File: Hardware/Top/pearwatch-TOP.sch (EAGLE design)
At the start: 49 parts, among them U2 NRF52832_MODULE_MDBT42, U4 PCF8523

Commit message: adding updated top board
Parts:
- added SW1, SW2: SWITCH.MOM, LinnesLab-Switches:SWITCH.MOM
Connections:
- net GND: now also USB2.SHIELD
- net N$5: now also C14.2, D1.A, R5.1
- net RESET: no longer C14.2, D1.A, R5.1
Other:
- note added: "Cortext Debugger"
- note added: "Digital Outputs CS.OLED RESET.OLED DC.OLED Digital Inputs 3x buttons Charge Status Analog Inputs Battery monitor Analog Outputs"
- note added: "Power Management"
- note added: "SD Card"
- note added: "buttons"
- note added: "nRF52832 Module"
- note added: "real time clock"
- note removed: "Additional notes for advanced users only"
- note removed: "PIN_DFU / P0.20: If this pin is detected to be at GND level at startup, the board will enter a special serial bootloader mode and will not execute any user code, going straight into bootloader mode. If you wish to use this pin as a standard GPIO, make sure that it is pulled high with a pullup resistor so that your code will execute normally when the MCU starts up. FRST/P0.22: Setting this pin to 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"
- note removed: "SPECIAL / PORT / PIN ON PACKAGE / GPIO(D_or_A) / Comments Factory Reset / P0.22 / pin38 / DO NOT USE FOR ANY GPIO SWDIO / none / pin37 / reserved-not available for general GPIO SWCLK / none / pin36 / reserved-not available for general GPIO RESET / P0.21 / pin35 / reserved-not available for general GPIO DFU / P0.20 / pin34 / reserved-not available for general GPIO LED2 / P0.19 / pin33 / reserved f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"
- note removed: "SPECIAL / PORT / PIN ON PACKAGE / GPIO(D_or_A) / Comments none / P0.02 / pin15 / D2_or_A0 none / P0.03 / pin16 / D3_or_A1 none / P0.04 / pin17 / D4_or_A2 none / P0.05 / pin18 / D5_or_A3 TXD / P0.06 / pin19 / D6 / but reserved for Serial communication and programming none / P0.07 / pin20 / D7 RXD / P0.08 / pin21 / D8 / but reserved for Serial communication and programming NFC1 / P0.09 / pin22 / D9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"
- note removed: "Some pins are noted as reserved and not available for general GPIO (unless you are an adavanced user) I2C, SPI, and SWD pins can be repurposed if you know what you are doing For Milestones, avoid repurposing NFC pins. For P0.19 (LED2), Adafruit's Bluetooth Low Energy libraries use this pin to indicated successful pairing. The LED blinks when the device is doing some Bluetooth process and stays li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"
- moved on the sheet: C10, C11, C12, C13, C14, C15, C16, C17, C18, C19, C2, C20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

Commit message: updating top board
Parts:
- removed C10, C11: 300p, LinnesLab-Passives:CAPACITOR0603
- removed C12: 10u, LinnesLab-Passives:CAPACITOR0805
- removed C13, C15, C17, C18, C19: 2.2uF, LinnesLab-Passives:CAPACITOR0402
- removed C14: 100n, LinnesLab-Passives:CAPACITOR0603
- removed C16: 10uF, LinnesLab-Passives:CAPACITOR0603
- removed CORTEX1: CORTEX_DEBUG_PTH, LinnesLab-Connectors:CORTEX_DEBUG_PTH
- removed D1: (no value), LinnesLab-DiscreteSemi:SCHOTTKY-USC
- removed L2: 10u, LinnesLab-Passives:INDUCTOR0603
- removed SW3, SW4: (no value), LinnesLab-Switches:SPST-PTS830GG140-COPY.1-3
- removed U4: PCF8523, LinnesLab-Clocks:PCF8523
- removed XTAL3: 32.7680kHz, LinnesLab-Clocks:CRYSTALECS-.327-12.5-12-C-TR
- added C25, C33, C35, C36, C37: 2.2uF, LinnesLab-Passives:CAPACITOR0402
- added C26: 1u, LinnesLab-Passives:CAPACITOR0603
- added C27, C28: (no value), LinnesLab-Passives:CAPACITOR0603
- added C29, C30: 300p, LinnesLab-Passives:CAPACITOR0603
- added C31: 10u, LinnesLab-Passives:CAPACITOR0805
- added C32: 100n, LinnesLab-Passives:CAPACITOR0603
- added C34: 10uF, LinnesLab-Passives:CAPACITOR0603
- added CORTEX3: CORTEX_DEBUG_PTH, LinnesLab-Connectors:CORTEX_DEBUG_PTH
- added D3: (no value), LinnesLab-DiscreteSemi:SCHOTTKY-USC
- added JP2: (no value), LinnesLab-Switches:JUMPER-SMT_2_NO_SILK
- added L3: 10u, LinnesLab-Passives:INDUCTOR0603
- added LED5: RED, LinnesLab-LED:LED0603
- added LED6: BLUE, LinnesLab-LED:LED0603
- added R10, R18: 10k, LinnesLab-Passives:RESISTOR0603
- added R16, R17, R20: 1k, LinnesLab-Passives:RESISTOR0603
- added R19: 390k, LinnesLab-Passives:RESISTOR0603
- added R21, R22: (no value), LinnesLab-Passives:RESISTOR0603
- added SW7, SW8: (no value), LinnesLab-Switches:SPST-PTS830GG140-COPY.1-3
- added U5: NRF52832_MODULE_MDBT42, LinnesLab-Microcontrollers:NRF52832_MODULE_MDBT42
- added U6: (no value), LinnesLab-Displays:DISP_OLED_UG-2864HSWEG01-NO-WRAPAROUND
- added XTAL4: 32.768kHz, LinnesLab-Clocks:CRYSTALECS-.327-12.5-12-C-TR
- C7: value 1u -> 100n
- C8, C9: value (none) -> 47p
- LED4: value BLUE -> YELLOW
- R3, R4: value 1k -> 10k
- R5, R6: value 10k -> 27
- R7: value 390k -> 1k
- R8, R9: value 10k -> 10K
- U2: value NRF52832_MODULE_MDBT42 -> FT231XS; device LinnesLab-Microcontrollers:NRF52832_MODULE_MDBT42 -> LinnesLab-DigitalIC:FT231XS
- U3: value (none) -> PCF8523; device LinnesLab-Displays:DISP_OLED_UG-2864HSWEG01-NO-WRAPAROUND -> LinnesLab-Clocks:PCF8523; DIGIKEY (none) -> 568-5306-1-ND; I2C_ADDRESS (none) -> 0x68h; MFN (none) -> PCF8523T/1,118; MFN_MANUFACTURER (none) -> NXP USA Inc.
- XTAL2: value 32.768kHz -> 32.7680kHz; FREQ (none) -> 32.7680KHZ
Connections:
- removed net N$10: LED4.A, R4.1
- removed net N$11: L2.1, U2.DCC
- removed net N$12: C7.1, L2.2, U2.DEC4
- removed net N$13: C16.2, U3.VCC
- removed net N$14: CORTEX1.NC/TDI
- removed net N$15: C18.2, U3.VCOMH
- removed net N$19: U4.OSCO, XTAL3.1
- removed net N$20: U4.OSCI, XTAL3.2
- removed net N$4: C8.2, U2.P0.00/XL1, XTAL2.1
- removed net N$5: C13.1, C14.2, D1.A, R5.1, U3.C2N
- removed net N$9: LED3.A, R3.1
- removed net RXD: U2.P0.08
- removed net TXD: U2.P0.06
- new net !CTS: JP2.2, U2.!CTS
- new net !DTR: U2.!DTR
- new net FT3V3: U2.3V3OUT
- new net N$18: R10.2, U6.BS1
- new net N$21: R19.1, U6.IREF
- new net N$23: C25.2, U6.C2P
- new net N$26: C27.2, U5.P0.00/XL1, XTAL4.1
- new net N$27: C28.1, U5.P0.01/XL2, XTAL4.2
- new net N$28: LED5.A, R16.1
- new net N$29: LED6.A, R17.1
- new net N$30: L3.1, U5.DCC
- new net N$31: C26.1, L3.2, U5.DEC4
- new net N$32: CORTEX3.NC/TDI
- new net N$33: C25.1, U6.C2N
- new net N$34: C33.2, U6.C1P
- new net N$35: C33.1, U6.C1N
- new net N$36: C34.2, U6.VCC
- new net N$37: C36.2, U6.VCOMH
- new net RXD.FT: U2.RXD
- new net RXD.NRF: R21.2, U5.P0.08
- new net RXDFT: R22.1
- new net RXLED: R7.1, U2.CBUS1
- new net TXD.FT: R21.1, U2.TXD
- new net TXD.NRF: R22.2, U5.P0.06
- new net TXLED: R20.1, U2.CBUS2
- net 3.3V: now also C31.2, C35.2, C37.2, C7.2, CORTEX3.VCC, D3.C, LED3.A, LED4.A, R18.2, R3.2, R4.2, U2.!RESET, U2.VCCIO, U5.VDD, U6.VBAT, U6.VDD; no longer C12.2, C17.2, C19.2, CORTEX1.VCC, D1.C, R5.2, U2.VDD, U3.VBAT, U4.VDD
- net CS.OLED: now also U6./CS; no longer U3./CS
- net DC.OLED: now also U6.DC/I2C_SA0; no longer U3.DC/I2C_SA0
- net DFU: now also SW7.B, U5.P0.20; no longer SW3.B, U2.P0.20
- net DTR: now also C32.1; no longer C14.1
- net FRST: now also U5.P0.22; no longer U2.P0.22
- net GND: now also C26.2, C27.1, C28.2, C29.2, C30.2, C31.1, C34.1, C35.1, C36.1, C37.1, C7.1, C8.2, C9.1, CORTEX3.GND@3, CORTEX3.GND@5, CORTEX3.GNDDTCT, CORTEX3.KEY, JP2.1, LED5.C, LED6.C, R10.1, R19.2, SW7.A, SW8.B, U2.GND@16, U2.GND@6, U5.GND@1, U5.GND@2, U5.GND@3, U5.GND@4, U6.BS0, U6.BS2, U6.NC(GND)@1, U6.NC(GND)@2, U6.VLSS, U6.VSS; no longer C10.2, C11.2, C12.1, C16.1, C17.1, C18.1, C19.1, C7.2, C8.1, C9.2, CORTEX1.GND@3, CORTEX1.GND@5, CORTEX1.GNDDTCT, CORTEX1.KEY, LED3.C, LED4.C, R6.1, R7.2, SW3.A, SW4.B, U2.GND@1, U2.GND@2, U2.GND@3, U2.GND@4, U3.BS0, U3.BS2, U3.NC(GND)@1, U3.NC(GND)@2, U3.VLSS, U4.VSS
- net LED1: now also R16.2, U5.P0.17; no longer R3.2, U2.P0.17
- net LED2: now also R17.2, U5.P0.19; no longer R4.2, U2.P0.19
- net MISO: now also U5.P0.14; no longer U2.P0.14
- net MOSI: now also U5.P0.13, U6.D1/SPI_SDIN/I2C_SDA; no longer U2.P0.13, U3.D1/SPI_SDIN/I2C_SDA
- net N$1: now also U3.OSCO, XTAL2.1; no longer R6.2, U3.BS1
- net N$2: now also U3.OSCI, XTAL2.2; no longer R7.1, U3.IREF
- net N$3: now also R5.2, U2.USBDM; no longer C13.2, U3.C2P
- net N$6: now also R6.2, U2.USBDP; no longer C9.1, U2.P0.01/XL2, XTAL2.2
- net N$7: now also LED3.C, R7.2; no longer C15.2, U3.C1P
- net N$8: now also LED4.C, R20.2; no longer C15.1, U3.C1N
- net P0.09/NFC1: now also C30.1, U5.P0.09; no longer C11.1, U2.P0.09
- net P0.10/NFC2: now also C29.1, U5.P0.10; no longer C10.1, U2.P0.10
- net RESET: now also C32.2, CORTEX3.!RESET, D3.A, R18.1, SW8.A, U5.P0.21/RESET; no longer CORTEX1.!RESET, SW4.A, U2.P0.21/RESET
- net RESET.OLED: now also U6./RES; no longer U3./RES
- net SCK: now also U5.P0.12, U6.D0/SPI_SCLK/I2C_SCK; no longer U2.P0.12, U3.D0/SPI_SCLK/I2C_SCK
- net SCL: now also R3.1, R9.1, U3.SCL, U5.P0.26; no longer R8.1, U2.P0.26, U4.SCL
- net SDA: now also R4.1, R8.1, U3.SDA, U5.P0.25; no longer R9.1, U2.P0.25, U4.SDA
- net SWCLK: now also CORTEX3.SWDCLK/TCK, U5.SWDCLK; no longer CORTEX1.SWDCLK/TCK, U2.SWDCLK
- net SWDIO: now also CORTEX3.SWDIO/TMS, U5.SWDIO; no longer CORTEX1.SWDIO/TMS, U2.SWDIO
- net SWO: now also CORTEX3.SWO/TDO, U5.P0.18/SWO; no longer CORTEX1.SWO/TDO, U2.P0.18/SWO
- net USB+: now also C8.1, R6.1
- net USB-: now also C9.2, R5.1
- net VBATT: now also U3.VBAT; no longer U4.VBAT
- net V_USB: now also U2.VCC
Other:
- note added: "Additional notes for advanced users only"
- note added: "I don't remember if CTS needs to be grounded or left floating so here's a jumper to ground so it can be configued either way dynamically."
- note added: "PIN_DFU / P0.20: If this pin is detected to be at GND level at startup, the board will enter a special serial bootloader mode and will not execute any user code, going straight into bootloader mode. If you wish to use this pin as a standard GPIO, make sure that it is pulled high with a pullup resistor so that your code will execute normally when the MCU starts up. FRST/P0.22: Setting this pin to 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"
- note added: "SPECIAL / PORT / PIN ON PACKAGE / GPIO(D_or_A) / Comments Factory Reset / P0.22 / pin38 / DO NOT USE FOR ANY GPIO SWDIO / none / pin37 / reserved-not available for general GPIO SWCLK / none / pin36 / reserved-not available for general GPIO RESET / P0.21 / pin35 / reserved-not available for general GPIO DFU / P0.20 / pin34 / reserved-not available for general GPIO LED2 / P0.19 / pin33 / reserved f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"
- note added: "SPECIAL / PORT / PIN ON PACKAGE / GPIO(D_or_A) / Comments none / P0.02 / pin15 / D2_or_A0 none / P0.03 / pin16 / D3_or_A1 none / P0.04 / pin17 / D4_or_A2 none / P0.05 / pin18 / D5_or_A3 TXD / P0.06 / pin19 / D6 / but reserved for Serial communication and programming none / P0.07 / pin20 / D7 RXD / P0.08 / pin21 / D8 / but reserved for Serial communication and programming NFC1 / P0.09 / pin22 / D9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"
- note added: "Some pins are noted as reserved and not available for general GPIO (unless you are an adavanced user) I2C, SPI, and SWD pins can be repurposed if you know what you are doing For Milestones, avoid repurposing NFC pins. For P0.19 (LED2), Adafruit's Bluetooth Low Energy libraries use this pin to indicated successful pairing. The LED blinks when the device is doing some Bluetooth process and stays li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"
- note added: "TXD goes to RX on the other device RXD goes to TX on the other device"
- moved on the sheet: C2, C7, C8, C9, LED3, LED4, R3, R4, R5, R6, R7, R8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

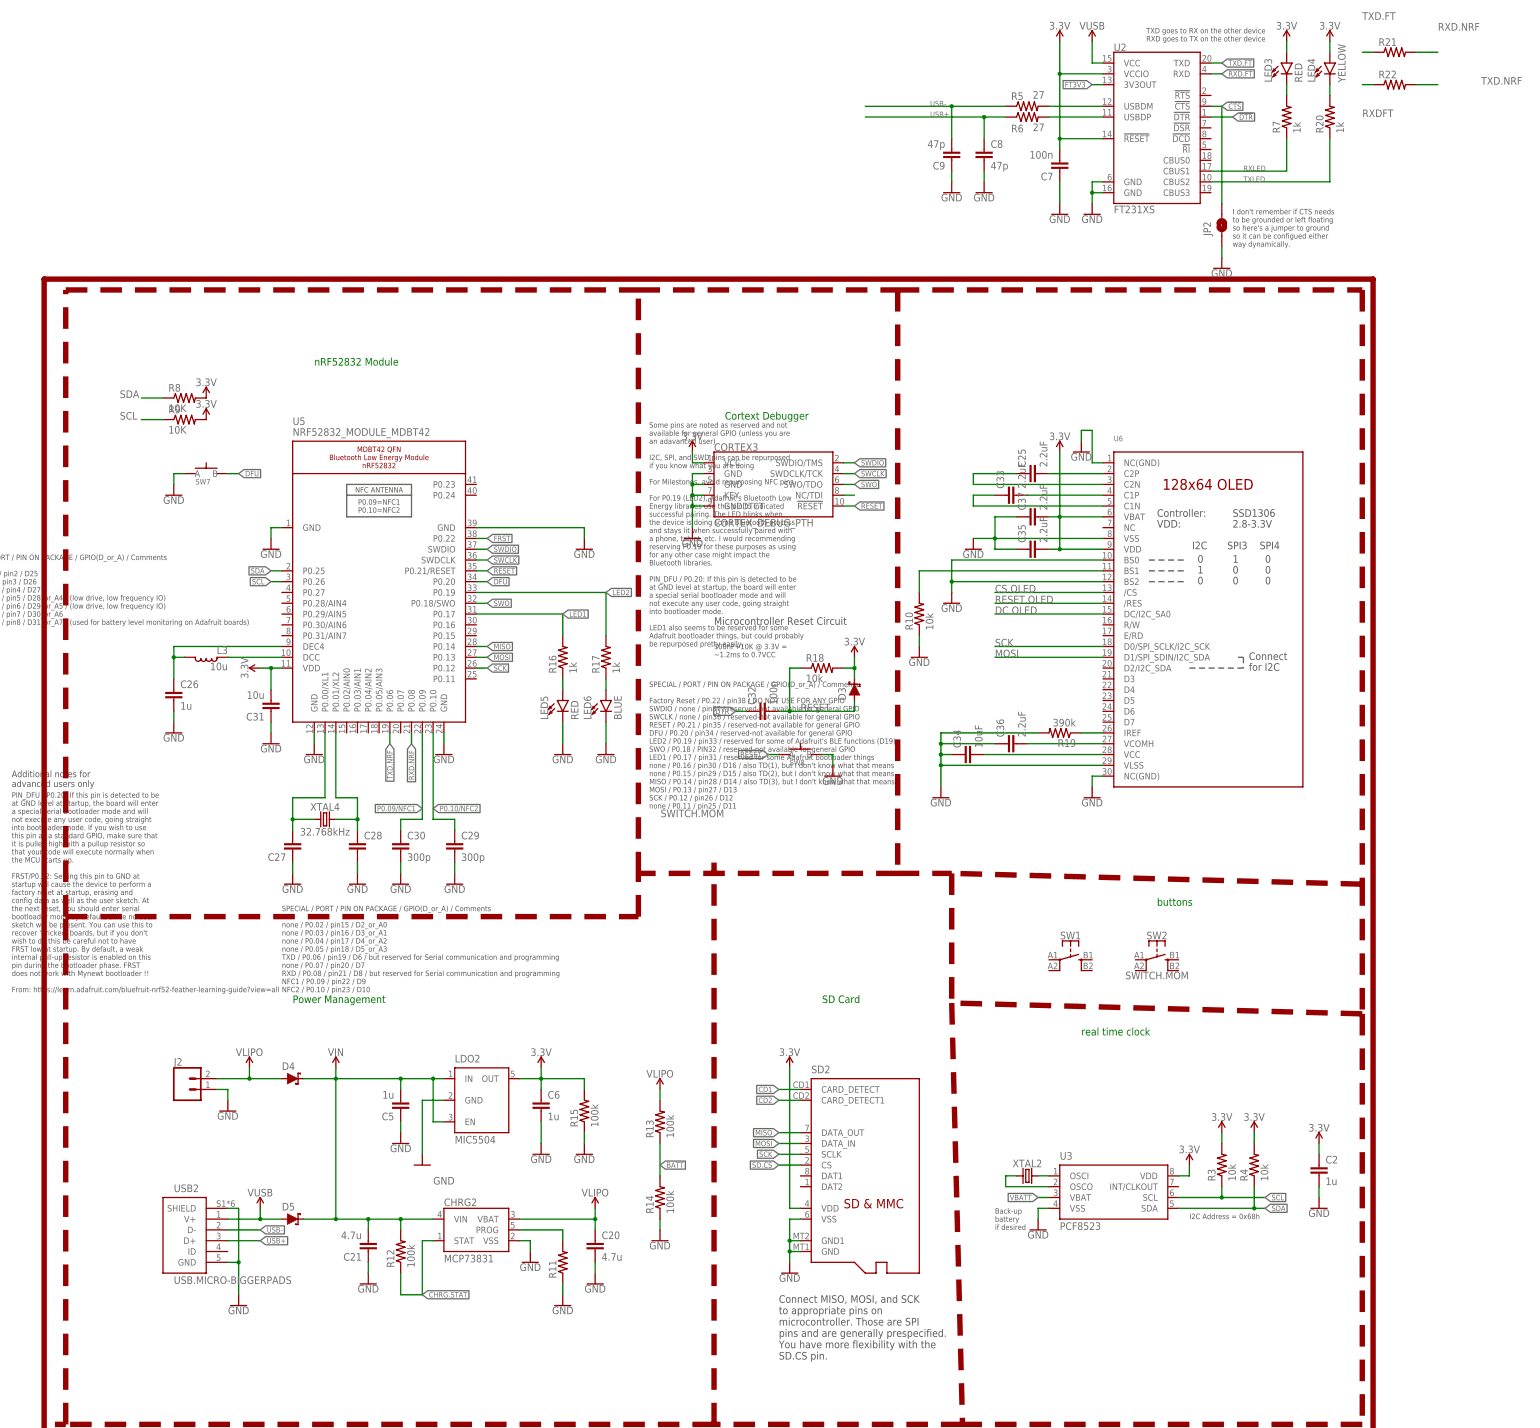
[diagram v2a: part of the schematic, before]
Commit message: deleted power management from top board
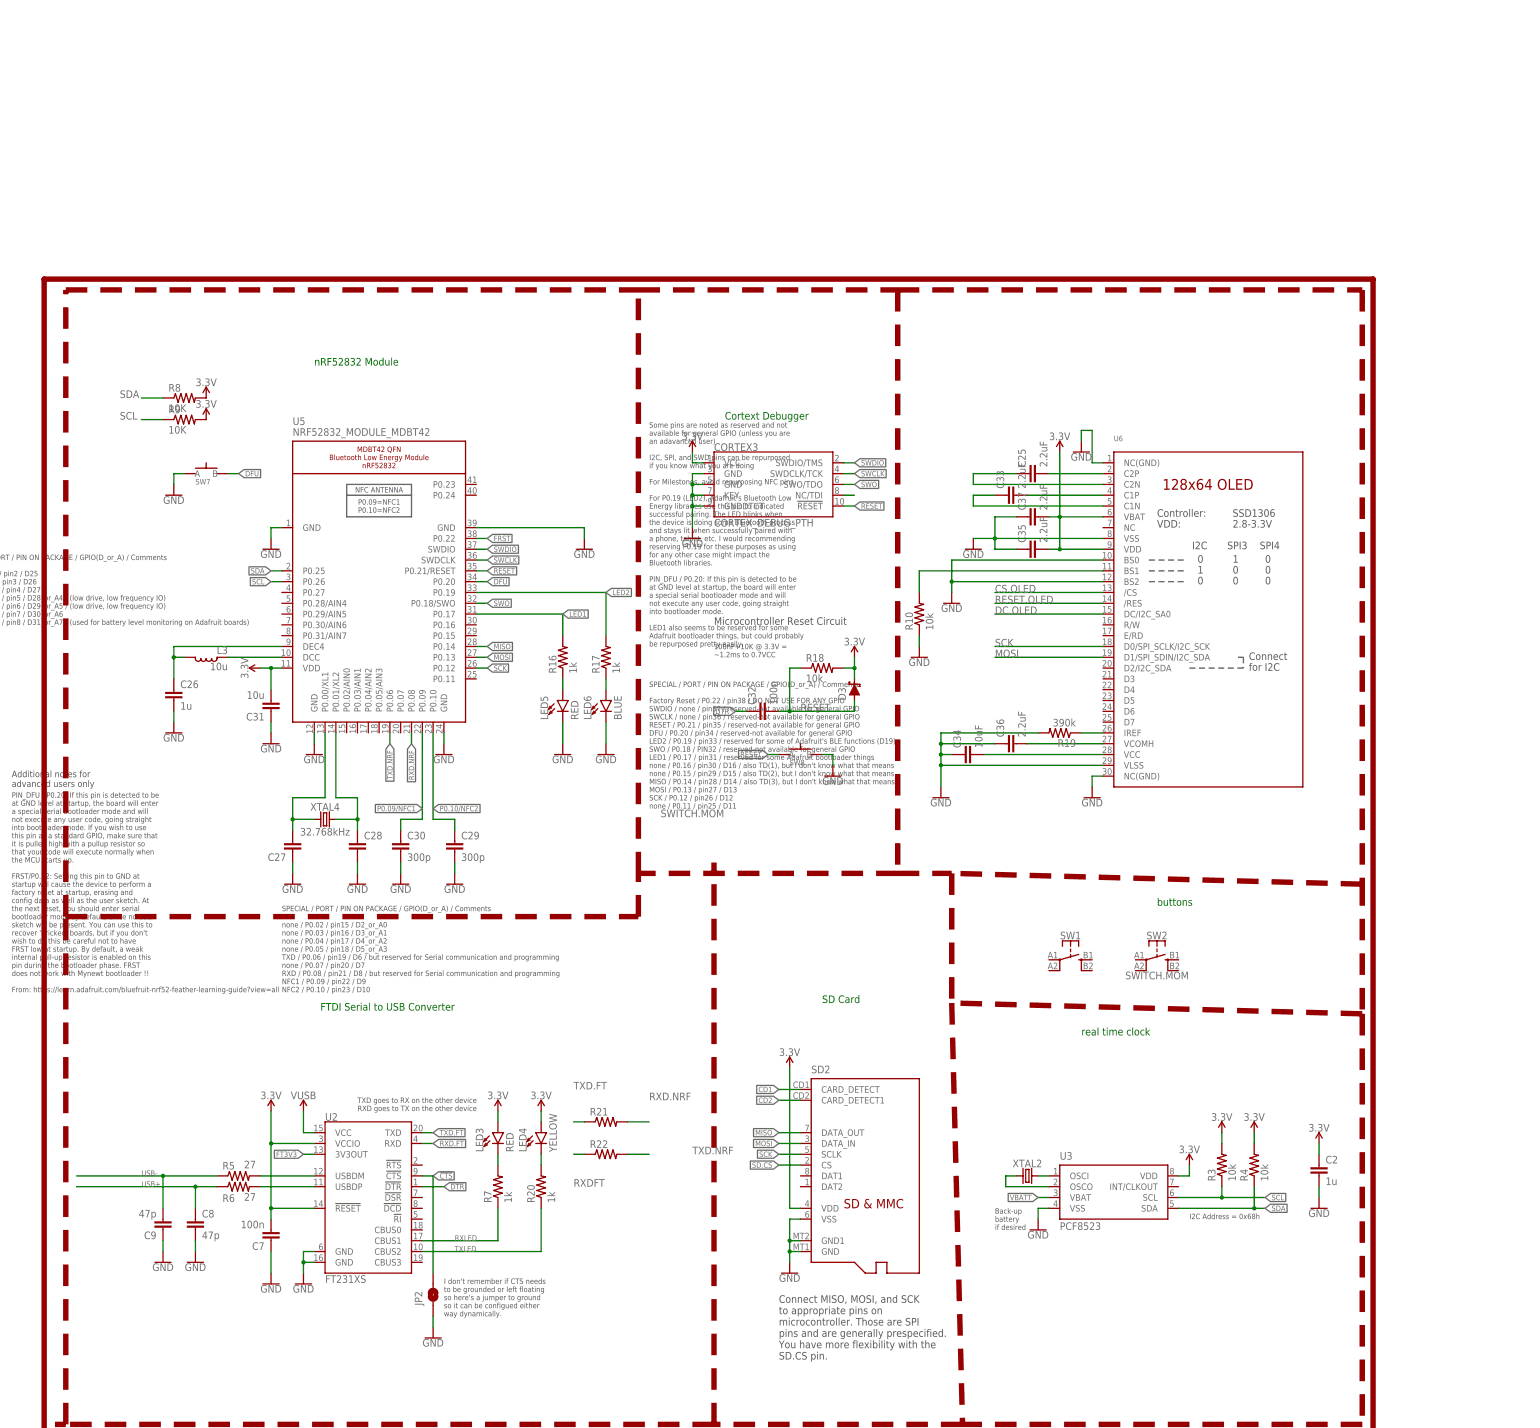
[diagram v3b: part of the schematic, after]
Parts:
- removed C20, C21: 4.7u, LinnesLab-Passives:CAPACITOR0603
- removed C5, C6: 1u, LinnesLab-Passives:CAPACITOR0603
- removed CHRG2: MCP73831, LinnesLab-Power:MCP73831
- removed D4, D5: (no value), LinnesLab-DiscreteSemi:SCHOTTKY-USC
- removed J2: (no value), LinnesLab-Connectors:CONN_02
- removed LDO2: MIC5504, LinnesLab-Power:MIC5504
- removed R11: (no value), LinnesLab-Passives:RESISTOR0603
- removed R12, R13, R14, R15: 100k, LinnesLab-Passives:RESISTOR0603
- removed USB2: USB.MICRO-BIGGERPADS, LinnesLab-Connectors:USB.MICRO-BIGGERPADS
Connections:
- removed net BATT: R13.1, R14.2
- removed net CHRG.STAT: CHRG2.STAT, R12.1
- removed net N$17: CHRG2.PROG, R11.2
- removed net VIN: C21.2, C5.2, CHRG2.VIN, D4.C, D5.C, LDO2.EN, LDO2.IN, R12.2
- removed net VLIPO: C20.1, CHRG2.VBAT, D4.A, J2.2, R13.2
- net 3.3V: no longer C6.1, LDO2.OUT, R15.2
- net GND: no longer C20.2, C21.1, C5.1, C6.2, CHRG2.VSS, J2.1, LDO2.GND, R11.1, R14.1, R15.1, USB2.GND, USB2.SHIELD
- net USB+: no longer USB2.D+
- net USB-: no longer USB2.D-
- net V_USB: no longer D5.A, USB2.V+
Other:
- note added: "FTDI Serial to USB Converter"
- note removed: "Power Management"
- moved on the sheet: C7, C8, C9, JP2, LED3, LED4, R20, R21, R22, R5, R6, R7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
